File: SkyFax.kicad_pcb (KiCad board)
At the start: 2 copper layers, 122.3 x 37.6 mm, 88 parts, among them J1 RJ11/12, J2 Conn_02x02_Odd_Even, J3 USB_B_Micro, J4 Conn_02x08_Odd_Even, J5 Conn_01x02, J6 Conn_01x02, Q1 Q_NPN_BEC, Q2 Q_PNP_BEC, Q3 Q_NPN_BEC, Q4 Q_NPN_BEC, Q5 Q_NPN_BEC, SW1 SW_Push, U1 Si2494-A-FM, U2 Si3018, U3 CP2102N-Axx-xQFN20, U4 25LC640AT-E/SN, U5 AZ1117-3.3, U6 74LCX541, U7 DS1818, X1 ECS-2520MV-xxx-xx

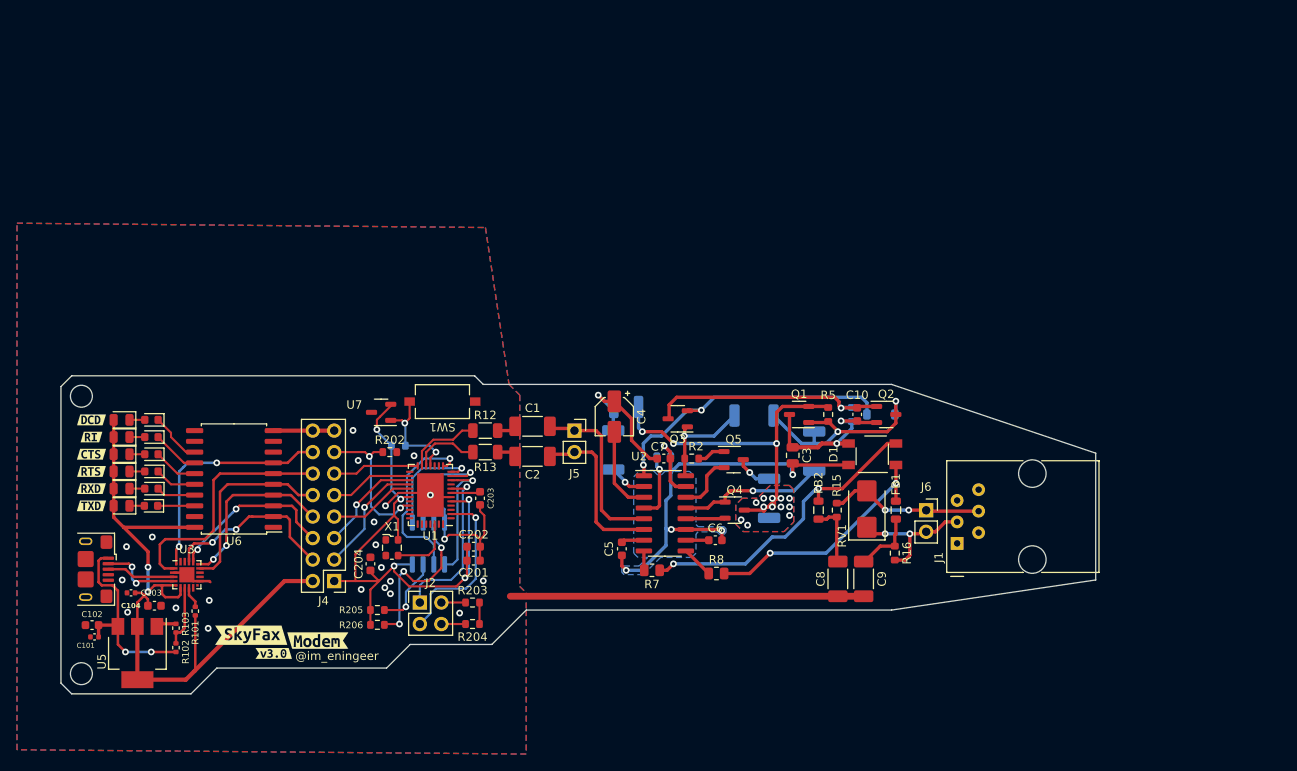
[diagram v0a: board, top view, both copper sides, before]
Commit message: [4.0] M.2 Module. Sent to fab
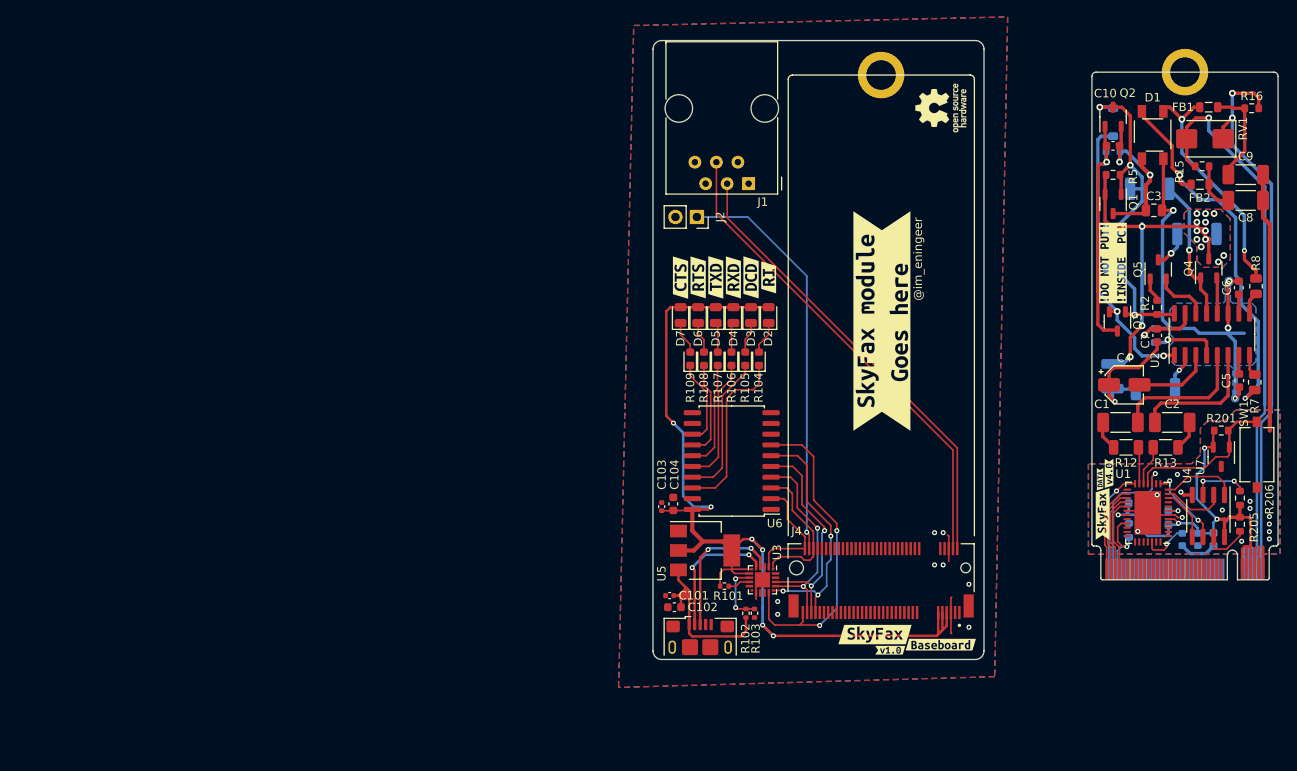
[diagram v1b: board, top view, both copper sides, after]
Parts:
- removed J5, J6: Conn_01x02, Connector_PinSocket_2.54mm:PinSocket_1x02_P2.54mm_Vertical
- removed R203, R204: 10k, Resistor_SMD:R_0603_1608Metric
- removed kibuzzard-64DEBF09: G***, kibuzzard-64DEBF09
- removed kibuzzard-64DEBF1B: G***, kibuzzard-64DEBF1B
- removed kibuzzard-64F3F98C: G***, kibuzzard-64F3F98C
- removed kibuzzard-64F3FC0B: G***, kibuzzard-64F3FC0B
- removed kibuzzard-64F3FC33: G***, kibuzzard-64F3FC33
- removed kibuzzard-64F3FC43: G***, kibuzzard-64F3FC43
- removed kibuzzard-64F3FC6A: G***, kibuzzard-64F3FC6A
- removed kibuzzard-64F3FC7E: G***, kibuzzard-64F3FC7E
- removed kibuzzard-64F3FC8A: G***, kibuzzard-64F3FC8A
- added J7: M.2_B_Edge, SkyFax:M.2-B-KEY_2260, F.Cu at (176.2, 131.0)
- added REF**: OSHW-Logo_5.7x6mm_SilkScreen, Symbol:OSHW-Logo_5.7x6mm_SilkScreen, F.Cu at (147.3, 75.3)
- added REF**: OSHW-Logo_5.7x6mm_SilkScreen, Symbol:OSHW-Logo_5.7x6mm_SilkScreen, B.Cu at (147.8, 135.5)
- added REF**: OSHW-Logo_5.7x6mm_SilkScreen, Symbol:OSHW-Logo_5.7x6mm_SilkScreen, B.Cu at (178.3, 77.0)
- added kibuzzard-650110F6: G***, kibuzzard-650110F6, F.Cu at (166.4, 123.3)
- added kibuzzard-65011101: G***, kibuzzard-65011101, F.Cu at (167.2, 118.5)
- added kibuzzard-650111BC: G***, kibuzzard-650111BC, B.Cu at (183.7, 76.4)
- added kibuzzard-650111C2: G***, kibuzzard-650111C2, B.Cu at (184.1, 82.0)
- added kibuzzard-650123DF: G***, kibuzzard-650123DF, F.Cu at (167.6, 93.6)
- added kibuzzard-650125E8: G***, kibuzzard-650125E8, F.Cu at (140.3, 100.5)
- added kibuzzard-6501311A: G***, kibuzzard-6501311A, F.Cu at (120.7, 95.3)
- added kibuzzard-65013126: G***, kibuzzard-65013126, F.Cu at (122.8, 95.3)
- added kibuzzard-6501314E: G***, kibuzzard-6501314E, F.Cu at (116.5, 95.3)
- added kibuzzard-6501315C: G***, kibuzzard-6501315C, F.Cu at (118.6, 95.3)
- added kibuzzard-6501316E: G***, kibuzzard-6501316E, F.Cu at (124.9, 95.3)
- added kibuzzard-6501317F: G***, kibuzzard-6501317F, F.Cu at (126.9, 95.3)
- added kibuzzard-6501337B: G***, kibuzzard-6501337B, F.Cu at (139.5, 137.5)
- added kibuzzard-6501337B: G***, kibuzzard-6501337B, B.Cu at (148.6, 107.4)
- added kibuzzard-65013388: G***, kibuzzard-65013388, F.Cu at (147.3, 138.7)
- added kibuzzard-65013388: G***, kibuzzard-65013388, B.Cu at (149.8, 115.2)
- added kibuzzard-650133AF: G***, kibuzzard-650133AF, F.Cu at (141.3, 139.4)
- added kibuzzard-650133AF: G***, kibuzzard-650133AF, B.Cu at (150.4, 109.2)
- added kibuzzard-65013408: G***, kibuzzard-65013408, F.Cu at (166.1, 119.2)
- C201, C202, C203, C204, R202, X1: moved to B.Cu
- J2: value Conn_02x02_Odd_Even -> Audio; footprint Connector_PinHeader_2.54mm:PinHeader_2x02_P2.54mm_Vertical -> Connector_PinSocket_2.54mm:PinSocket_1x02_P2.54mm_Vertical
- J4: value Conn_02x08_Odd_Even -> M.2_B_Connector; footprint Connector_PinHeader_2.54mm:PinHeader_2x08_P2.54mm_Vertical -> SkyFax:AMPHENOL_MDT420B01001_2260
- R201, U4: moved to F.Cu
- moved R206 103.0 mm to (182.7, 121.4), turned to 90 degrees
- moved R205 102.4 mm to (182.7, 124.5), turned to -90 degrees
- moved C204 99.7 mm to (179.5, 126.3), turned to 90 degrees
- moved U7 99.4 mm to (180.4, 116.5), turned to -90 degrees
- moved R201 97.3 mm to (180.4, 113.4)
- moved SW1 96.5 mm to (184.7, 116.3), turned to 90 degrees
- moved X1 94.3 mm to (176.8, 126.3), turned to 90 degrees
- moved U4 92.2 mm to (178.9, 123.5)
- moved R202 87.9 mm to (169.5, 125.2), turned to 90 degrees
- moved U1 84.8 mm to (171.8, 123.1)
- moved C201 81.5 mm to (173.4, 124.5), turned to 0 degrees
- moved C203 80.6 mm to (173.4, 122.9), turned to 0 degrees
- moved R13 80.4 mm to (173.9, 115.4)
- moved D2 79.7 mm to (126.9, 99.8), turned to 90 degrees
- moved C202 78.4 mm to (170.3, 122.0)
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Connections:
- J1 pad 3: /SI3018/TIP -> /USB_TIP
- J1 pad 4: /SI3018/RING -> /USB_RING
- J2 pad 1: /SI2494/SDI -> /USB_AOUT
- J2 pad 2: Net-(J2-Pin_2) -> GND
- J4 pad 1: +3V3 -> GND
- J4 pad 10: /USB_Serial/CTS -> GND
- J4 pad 11: /SI2494/nRI -> +3V3
- J4 pad 2: +3V3 -> /USB_TIP
- J4 pad 3: /SI2494/TXD -> GND
- J4 pad 4: /USB_Serial/TXD -> /USB_RING
- J4 pad 5: /SI2494/RXD -> GND
- J4 pad 6: /USB_Serial/RXD -> GND
- J4 pad 7: /SI2494/nRTS -> +3V3
- J4 pad 8: /USB_Serial/RTS -> GND
- J4 pad 9: /SI2494/nCTS -> +3V3
- R15 pad 2: /SI3018/RING -> /MOD_RING
- R16 pad 2: /SI3018/TIP -> /MOD_TIP
- R202 pad 1: /SI2494/nDCD -> /MOD_DCD
- RV1 pad 1: /SI3018/TIP -> /MOD_TIP
- RV1 pad 2: /SI3018/RING -> /MOD_RING
- U1 pad 15: unconnected-(U1-AOUT-Pad15) -> /MOD_AOUT
- U1 pad 19: /SI2494/nRI -> /MOD_RI
- U1 pad 2: /SI2494/nFSYNC -> unconnected-(U1-nFSYNC-Pad2)
- U1 pad 21: /SI2494/nCTS -> /MOD_CTS
- U1 pad 22: /SI2494/RXD -> /MOD_RXD
- U1 pad 23: /SI2494/TXD -> /MOD_TXD
- U1 pad 24: /SI2494/nRTS -> /MOD_RTS
- U1 pad 28: /SI2494/nDCD -> /MOD_DCD
- U1 pad 8: /SI2494/SDI -> unconnected-(U1-SDI-Pad8)
- U3 pad 1: /USB_Serial/DCD -> /USB_DCD
- U3 pad 15: /USB_Serial/CTS -> /USB_CTS
- U3 pad 16: /USB_Serial/RTS -> /USB_RTS
- U3 pad 17: /USB_Serial/RXD -> /USB_RXD
- U3 pad 18: /USB_Serial/TXD -> /USB_TXD
- U3 pad 2: /USB_Serial/RI -> /USB_RI
- U6 pad 2: /USB_Serial/TXD -> /USB_RI
- U6 pad 3: /USB_Serial/RXD -> /USB_DCD
- U6 pad 4: /USB_Serial/RTS -> /USB_RXD
- U6 pad 5: /USB_Serial/CTS -> /USB_TXD
- U6 pad 6: /USB_Serial/RI -> /USB_RTS
- U6 pad 7: /USB_Serial/DCD -> /USB_CTS
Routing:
- net /MOD_TIP: track 0.00 -> 66.2 mm, vias 0 -> 2
- net /MOD_RING: track 0.00 -> 64.8 mm, vias 0 -> 1
- net /USB_RING: track 0.00 -> 57.3 mm
- net /USB_TIP: track 0.00 -> 54.4 mm
- net /USB_AOUT: track 0.00 -> 48.2 mm, vias 0 -> 1
- net /USB_CTS: track 0.00 -> 38.6 mm, vias 0 -> 2
- net /USB_RTS: track 0.00 -> 29.6 mm, vias 0 -> 3
- net /USB_Serial/RI: track 29.2 -> 0.00 mm
- net /USB_Serial/DCD: track 27.8 -> 0.00 mm, vias 2 -> 0
- net /USB_TXD: track 0.00 -> 26.5 mm, vias 0 -> 2
- net /USB_RXD: track 0.00 -> 23.9 mm, vias 0 -> 2
- net /USB_Serial/CTS: track 22.8 -> 0.00 mm
- net /USB_Serial/RTS: track 21.1 -> 0.00 mm, vias 2 -> 0
- net /USB_Serial/TXD: track 21.0 -> 0.00 mm, vias 2 -> 0
- net /SI2494/nFSYNC: track 20.5 -> 0.00 mm, vias 1 -> 0
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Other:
- board size 122.3 x 37.6 mm -> 39.1 x 73.2 mm
- board text removed: "Intentionally left empty (DRC/ERC will fail here)"

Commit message: [4.1] Fix minor layout + BoM issue
X1, C204, R202 were too close to M.2 connector edge
Didn't realize one of the components were not included in the BoM (Q1,Q3)
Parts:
- removed kibuzzard-65011101: G***, kibuzzard-65011101
- removed kibuzzard-650111C2: G***, kibuzzard-650111C2
- added kibuzzard-6508DE31: G***, kibuzzard-6508DE31, F.Cu at (167.2, 118.5)
- added kibuzzard-6508DE41: G***, kibuzzard-6508DE41, B.Cu at (184.1, 82.0)
- moved C202 1.79 mm to (170.8, 120.3)
- moved X1 0.91 mm to (177.1, 125.4)
- moved R202 0.83 mm to (169.2, 124.5), turned to 0 degrees
- moved C204 0.77 mm to (179.5, 125.5)
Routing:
- net /MOD_DCD: track 9.08 -> 10.9 mm
- net GND: track 72.6 -> 71.2 mm, vias 21 -> 22
- net +3V3: track 167.4 -> 168.7 mm
- net Net-(U1-CLKIN_XTAL1): track 5.50 -> 6.46 mm

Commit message: [4.2] Sound card
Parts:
- removed kibuzzard-650133AF (x2): G***, kibuzzard-650133AF
- added kibuzzard-650CCF10: G***, kibuzzard-650CCF10, F.Cu at (141.3, 139.4)
- added kibuzzard-650CCF19: G***, kibuzzard-650CCF19, B.Cu at (150.4, 109.2)
- J2: footprint Connector_PinSocket_2.54mm:PinSocket_1x02_P2.54mm_Vertical -> Connector_PinSocket_2.54mm:PinSocket_1x03_P2.54mm_Vertical
- moved J2 2.78 mm to (120.4, 90.2)
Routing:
- net +3V3: track 168.7 -> 178.0 mm
- net /USB_AOUT: track 48.2 -> 45.5 mm
